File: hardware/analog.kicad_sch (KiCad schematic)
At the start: 31 parts, among them J3 73101-0570, U13 TLP3441TP_F, U14 ${SIM.PARAMS}, U15 ADG621BRMZ, U16 ${SIM.PARAMS}, U18 ${SIM.PARAMS}

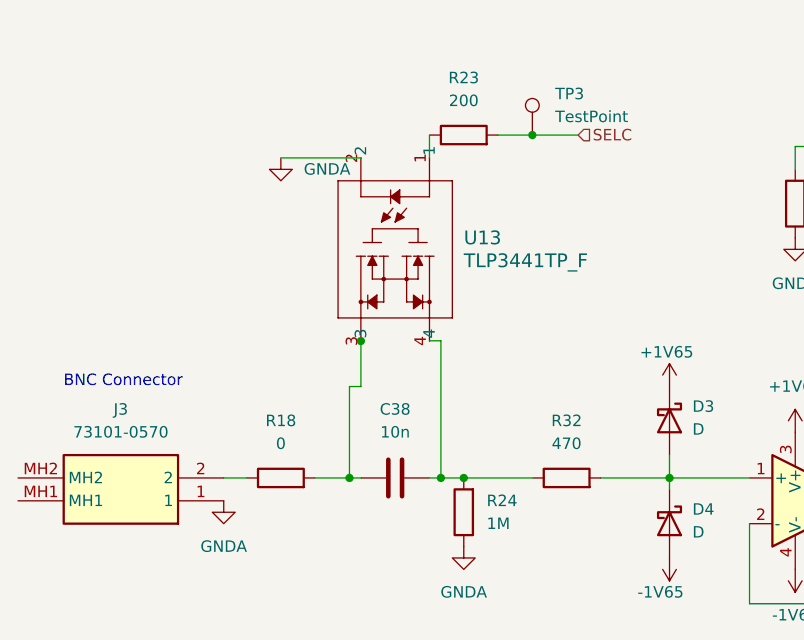
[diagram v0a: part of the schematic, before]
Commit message: feat(hardware): Fix disconnected analog block pins
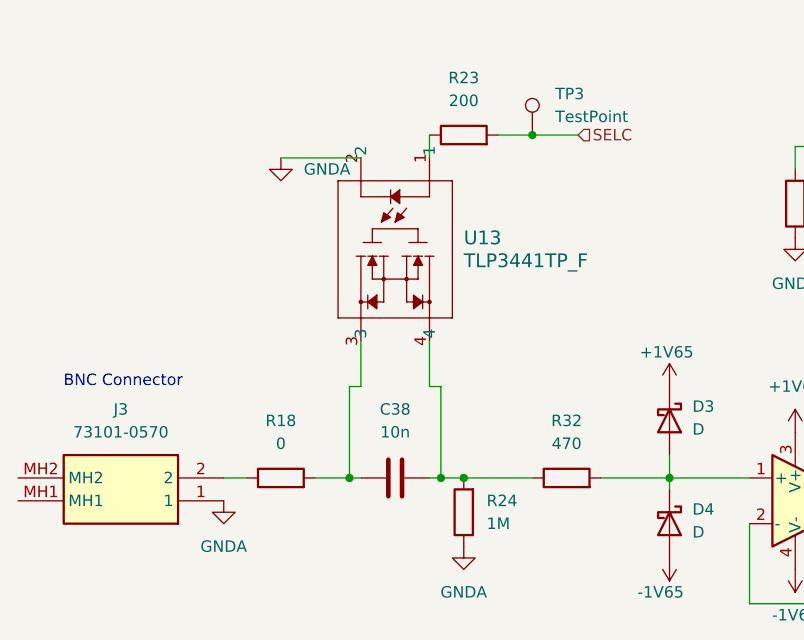
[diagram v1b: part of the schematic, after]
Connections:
- net GNDA: now also U13.2
- net at U13.1: now also R23.1
- net at U13.4: now also C38.2, R24.2, R32.1

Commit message: feat(hardware): Update switch footprint
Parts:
- R18: footprint Resistor_SMD:R_0402_1005Metric -> Resistor_SMD:R_0603_1608Metric
- TP1, TP3, TP5, TP7: Purchase Link (none) -> https://www.digikey.com/en/products/detail/koa-speer-electr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

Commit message: feat(hardware): Layout analog block 1
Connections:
- net at R26.1, U15.1 (S1), U15.7 (S2)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: no longer U15.6 (NC)
- no-connect marks 0 -> 1

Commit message: feat(hardware): updted design rules
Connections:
- net GNDA renamed GND

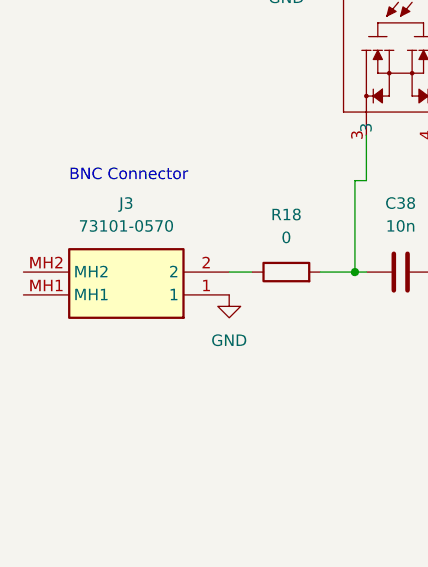
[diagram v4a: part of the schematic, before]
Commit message: feat(hardware): Connect bottom layer data lines
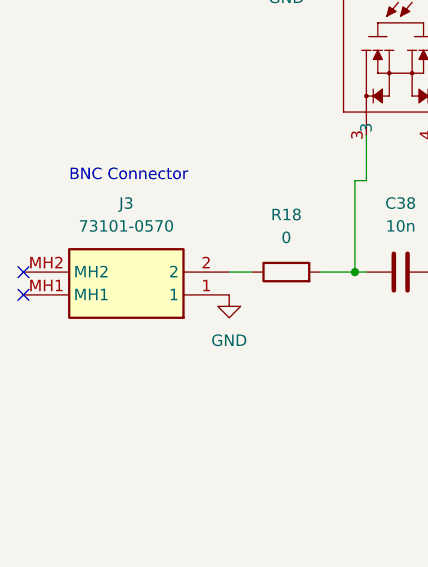
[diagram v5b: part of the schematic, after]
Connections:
- no-connect marks 1 -> 3

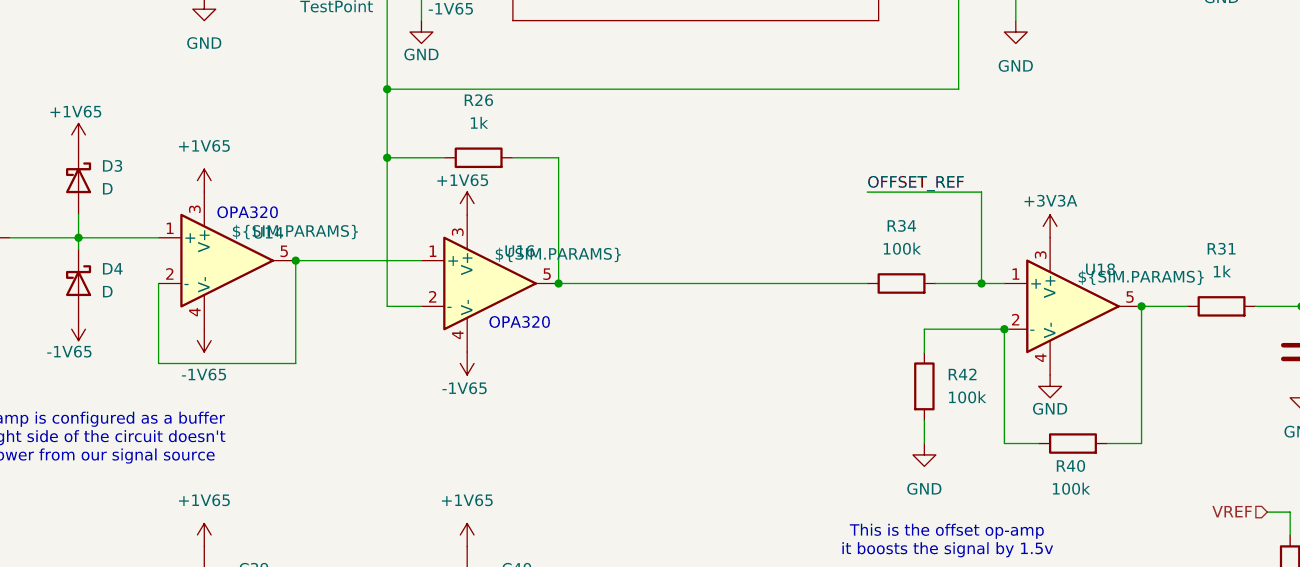
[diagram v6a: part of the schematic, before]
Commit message: changed pcb size, added pull up resistors to I2C, fixed OPA320 footprints/schematic
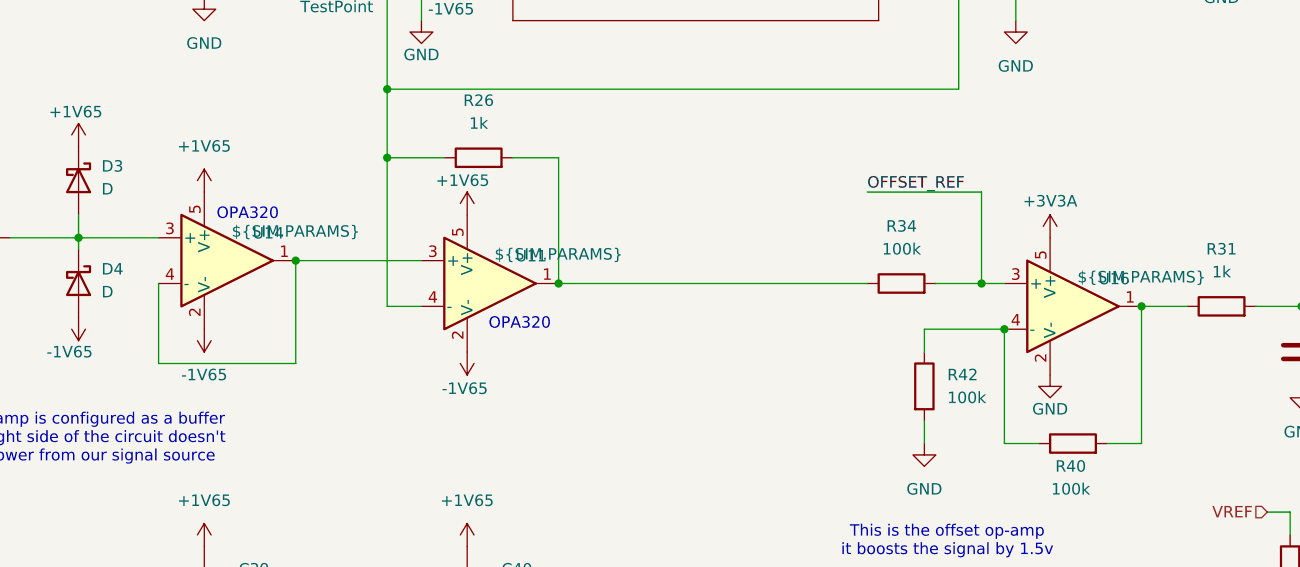
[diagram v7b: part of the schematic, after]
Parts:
- removed U18: ${SIM.PARAMS}, OPA320:DBV5, symbol Simulation_SPICE:OPAMP
- added U11: ${SIM.PARAMS}, OPA320:DBV5, symbol Simulation_SPICE:OPAMP
- U16: Purchase Link https://www.digikey.com/en/products/detail/texas-instrument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 -> (none)
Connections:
- net +1V65: now also U14.5 (V+), U11.5 (V+); no longer U14.3 (V+), U16.3 (V+)
- net +3V3A: now also U16.5 (V+)
- net -1V65: now also U14.2 (V-), U11.2 (V-); no longer U14.4 (V-), U16.4 (V-)
- net GND: now also U16.2 (V-)
- net OFFSET_REF: now also U16.3 (+)
- net at D3.2 (A), D4.1 (K), R32.2: now also U14.3 (+); no longer U14.1 (+)
- net at R26.1, U15.1 (S1), U15.7 (S2): now also U11.4 (-); no longer U16.2 (-)
- net at R26.2, R34.1: now also U11.1; no longer U16.5
- net at R40.1, R42.1: now also U16.4 (-)
- net at R31.1, R40.2: now also U16.1
- new net: U11.3 (+), U14.1, U14.4 (-)
